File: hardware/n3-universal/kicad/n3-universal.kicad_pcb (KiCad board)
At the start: 2 copper layers, 278 x 120 mm, 131 parts, among them J1 Bornier_5.08, J10 JST-XH, J11 Bornier_5.08, J12 Bornier_5.08, J13 Support OLED, J14 Support I2C ext, J15 Header servo, J16 Header servo, J17 Header service, J18 Bornier_5.08, J19 Bornier_5.08, J2 Jack 5.5/2.1, J20 Header alim, J21 Support I2C libre, J22 Support I2C libre, J23 Bornier_5.08, J24 Bornier_5.08, J25 Bornier_5.08, J26 Bornier_5.08, J27 Bornier_5.08, J28 Support I2C libre, J29 JST-XH, J3 Bornier_5.08, J30 JST-XH, J31 Bornier_5.08, J32 Bornier_5.08, J33 Bornier_5.08, J34 Bornier_5.08, J35 Support module microSD, J36 Bornier_5.08, J37 Bornier_5.08, J4 Bornier_5.08, J5 Bornier_5.08, J6 Bornier_5.08, J7 JST-XH, J8 JST-XH, J9 JST-XH, K1 SRD-05VDC-SL-C, K2 SRD-05VDC-SL-C, K3 SRD-05VDC-SL-C, K4 SRD-05VDC-SL-C, K5 SRD-05VDC-SL-C, K6 SRD-05VDC-SL-C, Q1 BC337-40, Q10 BC337-40, Q11 NDP6020P, Q2 BC337-40, Q3 BC337-40, Q4 BC337-40, Q5 BC337-40, Q6 BC337-40, Q7 NDP6020P, Q8 BC337-40, Q9 BS250

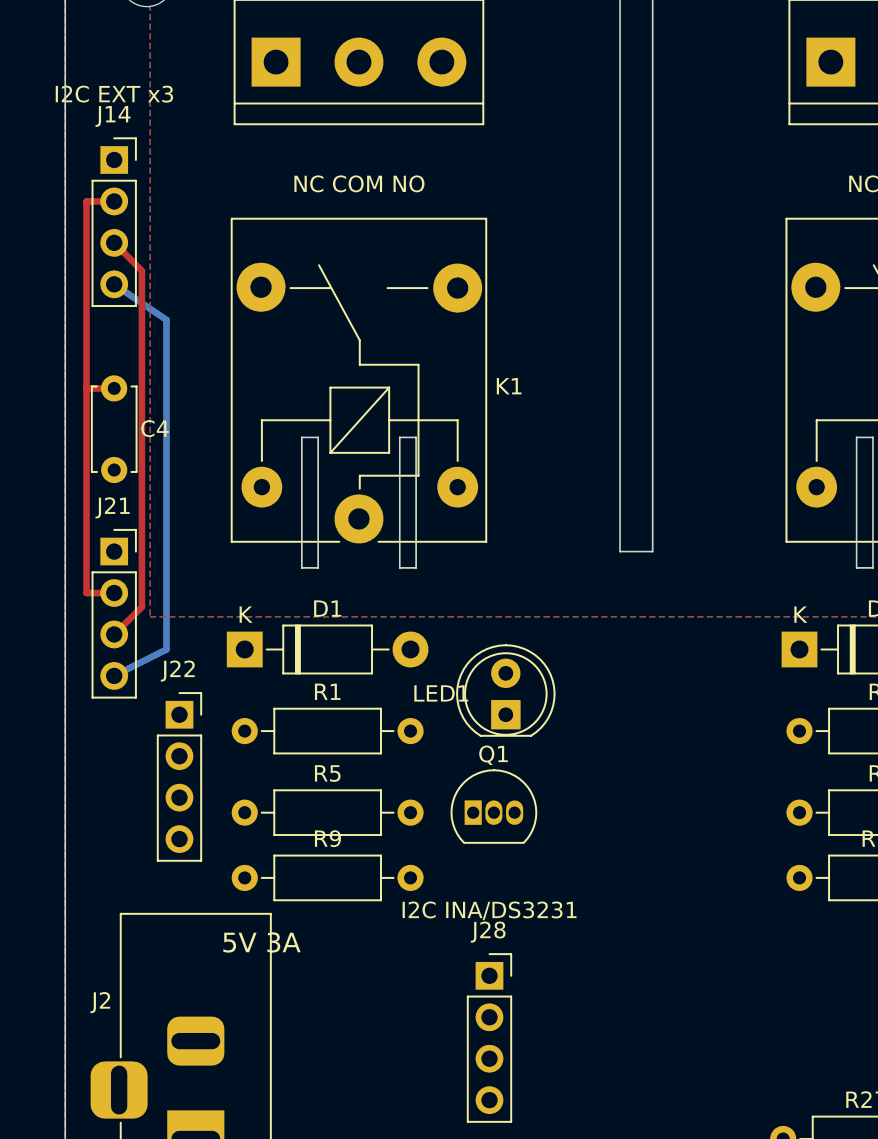
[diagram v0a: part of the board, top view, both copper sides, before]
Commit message: fix(n3-universal): J14/C4 relogés en zone médiane — supprime la cage de rails de la colonne gauche
La colonne x43 (J14/C4) exigeait des dorsales manuelles qui isolaient le GND
local (poche infranchissable des deux côtés). Reloger les deux composants à
côté de J28 dissout le problème : plus de rails, seeds réduits à l'échappée
EN, routage v7 en cours.

Co-Authored-By: Claude <noreply@anthropic.com>
Claude-Session: https://claude.ai/code/session_01HcxShQb65yktRwp31wBq9q
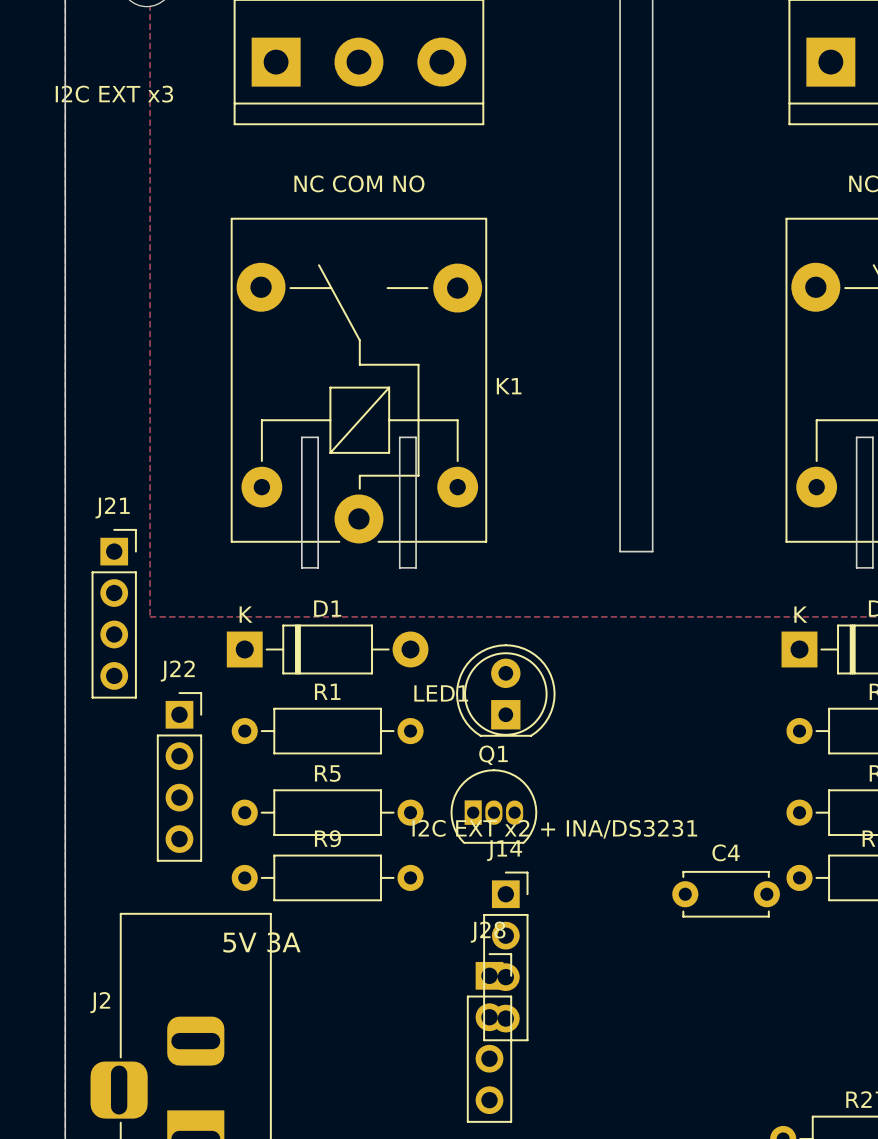
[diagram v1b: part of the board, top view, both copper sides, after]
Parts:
- moved J14 51.0 mm to (67.0, 101.0)
- moved C4 46.8 mm to (78.0, 101.0), turned to 0 degrees
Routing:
- net +3V3_SW: track 29.1 -> 0.00 mm
- net I2C_SDA: track 27.7 -> 0.00 mm
- net I2C_SCL: track 25.4 -> 0.00 mm
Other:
- board text added: "I2C EXT x2 + INA/DS3231"
- board text removed: "I2C INA/DS3231"
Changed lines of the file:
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@@
 	(footprint "n3u:PinSocket_1x04_P2.54mm_Vertical"
 		(layer "F.Cu")
-		(at 43 56)
+		(at 67 101)
 		(descr "Through hole straight socket strip, 1x04, 2.54mm pitch, single row (from Kicad 4.0.7), script generated")
 		(tags "Through hole socket strip THT 1x04 2.54mm single row")
@@
 			)
 		)
-		(fp_text user "K"
-			(at 0 -2.1 0)
+		(fp_text user "${REFERENCE}"
+			(at 5.47 0 0)
 			(layer "F.Fab")
 			(effects
@@
 			)
 		)
-		(fp_text user "${REFERENCE}"
-			(at 5.47 0 0)
+		(fp_text user "K"
+			(at 0 -2.1 0)
 			(layer "F.Fab")
 			(effects
@@
 			(layer "F.Fab")
 		)
-		(fp_text user "${REFERENCE}"
-			(at 7.1 0.025 0)
+		(fp_text user "1"
+			(at 0 -2.3 0)
 			(layer "F.Fab")
 			(effects
@@
 			)
 		)
-		(fp_text user "1"
-			(at 0 -2.3 0)
+		(fp_text user "${REFERENCE}"
+			(at 7.1 0.025 0)
 			(layer "F.Fab")
 			(effects
@@
 			)
 		)
-		(fp_text user "K"
-			(at 0 -2.1 0)
+		(fp_text user "${REFERENCE}"
+			(at 5.47 0 0)
 			(layer "F.Fab")
 			(effects
@@
 			)
 		)
-		(fp_text user "${REFERENCE}"
-			(at 5.47 0 0)
+		(fp_text user "K"
+			(at 0 -2.1 0)
 			(layer "F.Fab")
 			(effects
@@
 	(footprint "n3u:C_Disc_D5.0mm_W2.5mm_P5.00mm"
 		(layer "F.Cu")
-		(at 43 70 -90)
+		(at 78 101)
 		(descr "C, Disc series, Radial, pin pitch=5.00mm, , diameter*width=5*2.5mm^2, Capacitor, http://cdn-reichelt.de/documents/datenblatt/B300/DS_KERKO_TC.pdf")
 		(tags "C Disc series Radial pin pitch 5.00mm  diameter 5mm width 2.5mm Capacitor")
@@
 		(attr through_hole)
 		(fp_line
-			(start -0.12 1.37)
-			(end 5.12 1.37)
+			(start -0.12 -1.37)
+			(end -0.12 -1.055)
 			(stroke
 				(width 0.12)
@@
 		)
 		(fp_line
-			(start -0.12 1.055)
-			(end -0.12 1.37)
+			(start -0.12 -1.37)
+			(end 5.12 -1.37)
 			(stroke
 				(width 0.12)
@@
 		)
 		(fp_line
-			(start 5.12 1.055)
-			(end 5.12 1.37)
+			(start -0.12 1.055)
+			(end -0.12 1.37)
 			(stroke
 				(width 0.12)
@@
 		)
 		(fp_line
-			(start -0.12 -1.37)
-			(end -0.12 -1.055)
+			(start -0.12 1.37)
+			(end 5.12 1.37)
 			(stroke
 				(width 0.12)
@@
 		)
 		(fp_line
-			(start -0.12 -1.37)
-			(end 5.12 -1.37)
+			(start 5.12 -1.37)
+			(end 5.12 -1.055)
 			(stroke
 				(width 0.12)
@@
 		)
 		(fp_line
-			(start 5.12 -1.37)
-			(end 5.12 -1.055)
+			(start 5.12 1.055)
+			(end 5.12 1.37)
 			(stroke
 				(width 0.12)
@@
 		)
 		(fp_line
-			(start -1.05 1.5)
-			(end 6.05 1.5)
+			(start -1.05 -1.5)
+			(end -1.05 1.5)
 			(stroke
 				(width 0.05)
@@
 		)
 		(fp_line
-			(start 6.05 1.5)
-			(end 6.05 -1.5)
+			(start -1.05 1.5)
+			(end 6.05 1.5)
 			(stroke
 				(width 0.05)
@@
 		)
 		(fp_line
-			(start -1.05 -1.5)
-			(end -1.05 1.5)
+			(start 6.05 -1.5)
+			(end -1.05 -1.5)
 			(stroke
 				(width 0.05)
@@
 		)
 		(fp_line
-			(start 6.05 -1.5)
-			(end -1.05 -1.5)
+			(start 6.05 1.5)
+			(end 6.05 -1.5)
 			(stroke
 				(width 0.05)
@@
 		)
 		(fp_line
-			(start 0 1.25)
-			(end 5 1.25)
+			(start 0 -1.25)
+			(end 0 1.25)
 			(stroke
 				(width 0.1)
@@
 		)
 		(fp_line
-			(start 5 1.25)
-			(end 5 -1.25)
+			(start 0 1.25)
+			(end 5 1.25)
 			(stroke
 				(width 0.1)
@@
 		)
 		(fp_line
-			(start 0 -1.25)
-			(end 0 1.25)
+			(start 5 -1.25)
+			(end 0 -1.25)
 			(stroke
 				(width 0.1)
@@
 		)
 		(fp_line
-			(start 5 -1.25)
-			(end 0 -1.25)
+			(start 5 1.25)
+			(end 5 -1.25)
 			(stroke
 				(width 0.1)
@@
 		)
 		(pad "1" thru_hole circle
-			(at 0 0 270)
+			(at 0 0)
 			(size 1.6 1.6)
 			(drill 0.8)
@@
 		)
 		(pad "2" thru_hole circle
-			(at 5 0 270)
+			(at 5 0)
 			(size 1.6 1.6)
 			(drill 0.8)
@@
 			)
 		)
-		(fp_text user "${REFERENCE}"
-			(at 5.47 0 0)
+		(fp_text user "K"
+			(at 0 -2.1 0)
 			(layer "F.Fab")
 			(effects
@@
 			)
 		)
-		(fp_text user "K"
-			(at 0 -2.1 0)
+		(fp_text user "${REFERENCE}"
+			(at 5.47 0 0)
 			(layer "F.Fab")
 			(effects
@@
 			(layer "F.Fab")
 		)
-		(fp_text user "1"
-			(at 0 -2.3 0)
+		(fp_text user "${REFERENCE}"
+			(at 7.1 0.025 0)
 			(layer "F.Fab")
 			(effects
@@
 			)
 		)
-		(fp_text user "${REFERENCE}"
-			(at 7.1 0.025 0)
+		(fp_text user "1"
+			(at 0 -2.3 0)
 			(layer "F.Fab")
 			(effects
@@
 		)
 	)
-	(gr_text "I2C INA/DS3231"
-		(at 66 102 0)
+	(gr_text "I2C EXT x2 + INA/DS3231"
+		(at 70 97 0)
 		(layer "F.SilkS")
 		(effects
@@
 	)
 	(segment
-		(start 43 58.54)
-		(end 41.3 58.54)
-		(width 0.4)
-		(layer "F.Cu")
-		(net 2)
-	)
-	(segment
-		(start 41.3 58.54)
-		(end 41.3 70)
-		(width 0.4)
-		(layer "F.Cu")
-		(net 2)
-	)
-	(segment
-		(start 41.3 70)
-		(end 43 70)
-		(width 0.4)
-		(layer "F.Cu")
-		(net 2)
-	)
-	(segment
-		(start 41.3 70)
-		(end 41.3 82.54)
-		(width 0.4)
-		(layer "F.Cu")
-		(net 2)
-	)
-	(segment
-		(start 41.3 82.54)
-		(end 43 82.54)
-		(width 0.4)
-		(layer "F.Cu")
-		(net 2)
-	)
-	(segment
 		(start 96.5 110)
 		(end 100 110)
@@
 		(net 11)
 	)
-	(segment
-		(start 43 61.08)
-		(end 44.7 62.8)
-		(width 0.4)
-		(layer "F.Cu")
-		(net 16)
-	)
-	(segment
-		(start 44.7 83.4)
-		(end 43 85.08)
-		(width 0.4)
-		(layer "F.Cu")
-		(net 16)
-	)
-	(segment
-		(start 44.7 62.8)
-		(end 44.7 83.4)
-		(width 0.4)
-		(layer "F.Cu")
-		(net 16)
-	)
-	(segment
-		(start 43 63.62)
-		(end 46.2 65.8)
-		(width 0.4)
-		(layer "B.Cu")
-		(net 17)
-	)
-	(segment
-		(start 46.2 65.8)
-		(end 46.2 86)
-		(width 0.4)
-		(layer "B.Cu")
-		(net 17)
-	)
-	(segment
-		(start 46.2 86)
-		(end 43 87.62)
-		(width 0.4)
-		(layer "B.Cu")
-		(net 17)
-	)
 	(zone

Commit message: fix(n3-universal): J14 (74,106) / C4 (80,108) — les supports 1x04 s'étendent en +y (imbrication de perçages avec J28 corrigée)
Co-Authored-By: Claude <noreply@anthropic.com>
Claude-Session: https://claude.ai/code/session_01HcxShQb65yktRwp31wBq9q
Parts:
- moved J14 8.60 mm to (74.0, 106.0)
- moved C4 7.28 mm to (80.0, 108.0)
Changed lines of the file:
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@@
 	(footprint "n3u:PinSocket_1x04_P2.54mm_Vertical"
 		(layer "F.Cu")
-		(at 67 101)
+		(at 74 106)
 		(descr "Through hole straight socket strip, 1x04, 2.54mm pitch, single row (from Kicad 4.0.7), script generated")
 		(tags "Through hole socket strip THT 1x04 2.54mm single row")
@@
 			)
 		)
-		(fp_text user "${REFERENCE}"
-			(at 5.47 0 0)
+		(fp_text user "K"
+			(at 0 -2.1 0)
 			(layer "F.Fab")
 			(effects
@@
 			)
 		)
-		(fp_text user "K"
-			(at 0 -2.1 0)
+		(fp_text user "${REFERENCE}"
+			(at 5.47 0 0)
 			(layer "F.Fab")
 			(effects
@@
 			)
 		)
-		(fp_text user "${REFERENCE}"
-			(at 5.47 0 0)
+		(fp_text user "K"
+			(at 0 -2.1 0)
 			(layer "F.Fab")
 			(effects
@@
 			)
 		)
-		(fp_text user "K"
-			(at 0 -2.1 0)
+		(fp_text user "${REFERENCE}"
+			(at 5.47 0 0)
 			(layer "F.Fab")
 			(effects
@@
 			(layer "F.Fab")
 		)
-		(fp_text user "1"
-			(at 0 -2.3 0)
+		(fp_text user "${REFERENCE}"
+			(at 7.1 0.025 0)
 			(layer "F.Fab")
 			(effects
@@
 			)
 		)
-		(fp_text user "${REFERENCE}"
-			(at 7.1 0.025 0)
+		(fp_text user "1"
+			(at 0 -2.3 0)
 			(layer "F.Fab")
 			(effects
@@
 			(layer "F.CrtYd")
 		)
-		(fp_text user "ANTENNE"
-			(at 11.43 -7 0)
+		(fp_text user "USB"
+			(at 11.43 57 0)
 			(layer "F.SilkS")
 			(effects
@@
 			)
 		)
-		(fp_text user "USB"
-			(at 11.43 57 0)
+		(fp_text user "ANTENNE"
+			(at 11.43 -7 0)
 			(layer "F.SilkS")
 			(effects
@@
 			)
 		)
-		(fp_text user "K"
-			(at 0 -2.1 0)
+		(fp_text user "${REFERENCE}"
+			(at 5.47 0 0)
 			(layer "F.Fab")
 			(effects
@@
 			)
 		)
-		(fp_text user "${REFERENCE}"
-			(at 5.47 0 0)
+		(fp_text user "K"
+			(at 0 -2.1 0)
 			(layer "F.Fab")
 			(effects
@@
 			(layer "F.CrtYd")
 		)
-		(fp_text user "ANTENNE"
-			(at 12.7 -4.5 0)
+		(fp_text user "USB"
+			(at 12.7 37.5 0)
 			(layer "F.SilkS")
 			(effects
@@
 			)
 		)
-		(fp_text user "USB"
-			(at 12.7 37.5 0)
+		(fp_text user "ANTENNE"
+			(at 12.7 -4.5 0)
 			(layer "F.SilkS")
 			(effects
@@
 	(footprint "n3u:C_Disc_D5.0mm_W2.5mm_P5.00mm"
 		(layer "F.Cu")
-		(at 78 101)
+		(at 80 108)
 		(descr "C, Disc series, Radial, pin pitch=5.00mm, , diameter*width=5*2.5mm^2, Capacitor, http://cdn-reichelt.de/documents/datenblatt/B300/DS_KERKO_TC.pdf")
 		(tags "C Disc series Radial pin pitch 5.00mm  diameter 5mm width 2.5mm Capacitor")
@@
 			)
 		)
-		(fp_text user "K"
-			(at 0 -2.6 0)
+		(fp_text user "${REFERENCE}"
+			(at 8.3325 0 0)
 			(layer "F.Fab")
 			(effects
@@
 			)
 		)
-		(fp_text user "${REFERENCE}"
-			(at 8.3325 0 0)
+		(fp_text user "K"
+			(at 0 -2.6 0)
 			(layer "F.Fab")
 			(effects
@@
 			(layer "F.Fab")
 		)
-		(fp_text user "${REFERENCE}"
-			(at 7.1 0.025 0)
+		(fp_text user "1"
+			(at 0 -2.3 0)
 			(layer "F.Fab")
 			(effects
@@
 			)
 		)
-		(fp_text user "1"
-			(at 0 -2.3 0)
+		(fp_text user "${REFERENCE}"
+			(at 7.1 0.025 0)
 			(layer "F.Fab")
 			(effects

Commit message: feat(n3-universal): carte routée et validée — DRC 0/0/0, 3mm 0, livrables complets (rev 0.1)
Routage final (freerouting + secteur en dur + amorce EN + couture GND) :
DRC 0 violation / 0 pad non connecté / 0 erreur d'empreinte, contrôle 3 mm
indépendant 0 écart, ERC 0, garde anti-dérive vert (3 firmwares × 2 sites),
sérigraphie 0 conflit après tidy. Livrables : gerbers v0.1 (zip 10 fichiers,
PTH 520 + NPTH 4, marqueur JLCJLCJLCJLC au dos), schema.pdf, SVG avant/arrière/
sérigraphie, BOM complétée (supports 1x22, modules microSD/DS3231/INA/buck).
Docs : index hardware, VERIFICATION.md (section n3-universal), COMMANDE_JLCPCB
(2 oz obligatoire). J14/C4 relogés en zone médiane (leçon de routage : la
colonne gauche était infranchissable).

Co-Authored-By: Claude <noreply@anthropic.com>
Claude-Session: https://claude.ai/code/session_01HcxShQb65yktRwp31wBq9q
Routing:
- net GND: track 0.00 -> 912.5 mm, vias 0 -> 46
- net +5V: track 0.00 -> 758.2 mm
- net +3V3_SW: track 0.00 -> 538.8 mm
- net I2C_SCL: track 0.00 -> 297.4 mm, vias 0 -> 5
- net I2C_SDA: track 0.00 -> 276.1 mm, vias 0 -> 3
- net +3V3: track 0.00 -> 252.1 mm, vias 0 -> 1
- net K1: track 0.00 -> 251.0 mm, vias 0 -> 3
- net ADC_A: track 0.00 -> 250.3 mm, vias 0 -> 3
- net EN: track 3.50 -> 252.1 mm
- net K6: track 0.00 -> 244.2 mm, vias 0 -> 4
- net ONEWIRE: track 0.00 -> 238.1 mm, vias 0 -> 1
- net ADC_B: track 0.00 -> 236.9 mm, vias 0 -> 2
- net K3: track 0.00 -> 236.7 mm, vias 0 -> 5
- net SPARE_RX0: track 0.00 -> 231.4 mm, vias 0 -> 3
- net SPARE_TX0: track 0.00 -> 230.0 mm, vias 0 -> 1
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
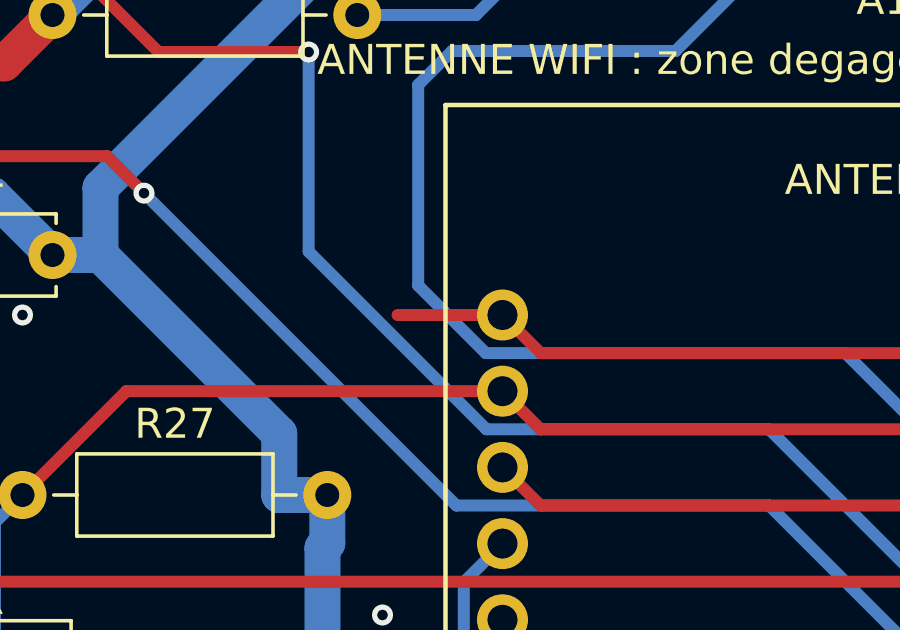
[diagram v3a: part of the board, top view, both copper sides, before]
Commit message: chore(n3-universal): revue finale — amorce EN flottante retirée, manifest complété, doc wroom-sd clarifiée
Revue complète avant livraison :
- PCB : suppression de l'amorce de routage EN (96,5→100 ; 110) devenue inutile
  (pad A1-30 raccordé par ailleurs) — seul warning track_dangling de la carte.
  DRC re-vérifiée : 0 erreur / 0 non-connecté / 0 empreinte ; contrôle 3 mm : 0 écart ;
  garde anti-dérive OK. Gerbers v0.1 + PDF/SVG régénérés (zip 10 fichiers, PTH 520 + NPTH 4).
- firmwares.manifest.json : catalogue des envs complété — esp32dev_universal_test (msp, n3pp),
  wroom-universal-test, wroom-s3-universal-test, plus wroom-s3-carrier-test (oubli de la
  carte ffp5cs rev 0.6) et wroom-beta-local (lacune préexistante).
- README n3-universal : wroom-sd explicitement marqué « futur env à créer »
  (aligné sur ffp5cs/VERSION.md ; seules les constantes SD existent dans pins.h).
- Builds re-vérifiés : msp et n3pp esp32dev_universal_test SUCCESS.

Co-Authored-By: Claude <noreply@anthropic.com>
Claude-Session: https://claude.ai/code/session_01HcxShQb65yktRwp31wBq9q
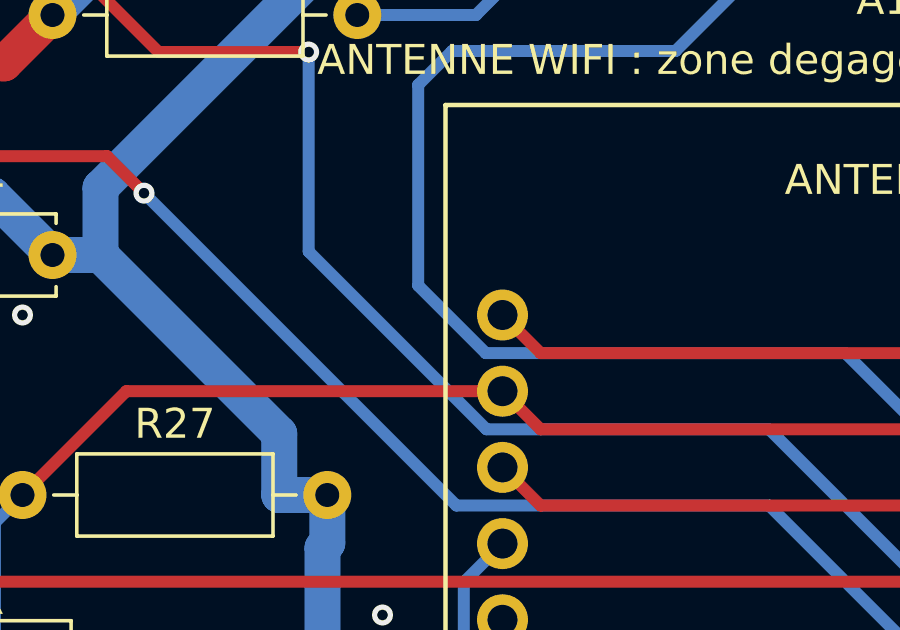
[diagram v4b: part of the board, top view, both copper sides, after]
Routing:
- net EN: track 252.1 -> 248.6 mm
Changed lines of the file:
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@@
-	)
-	(segment
-		(start 96.5 110)
-		(end 100 110)
-		(width 0.4)
-		(layer "F.Cu")
-		(net 11)
 	)
 	(segment
